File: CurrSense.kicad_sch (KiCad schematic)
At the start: 13 parts

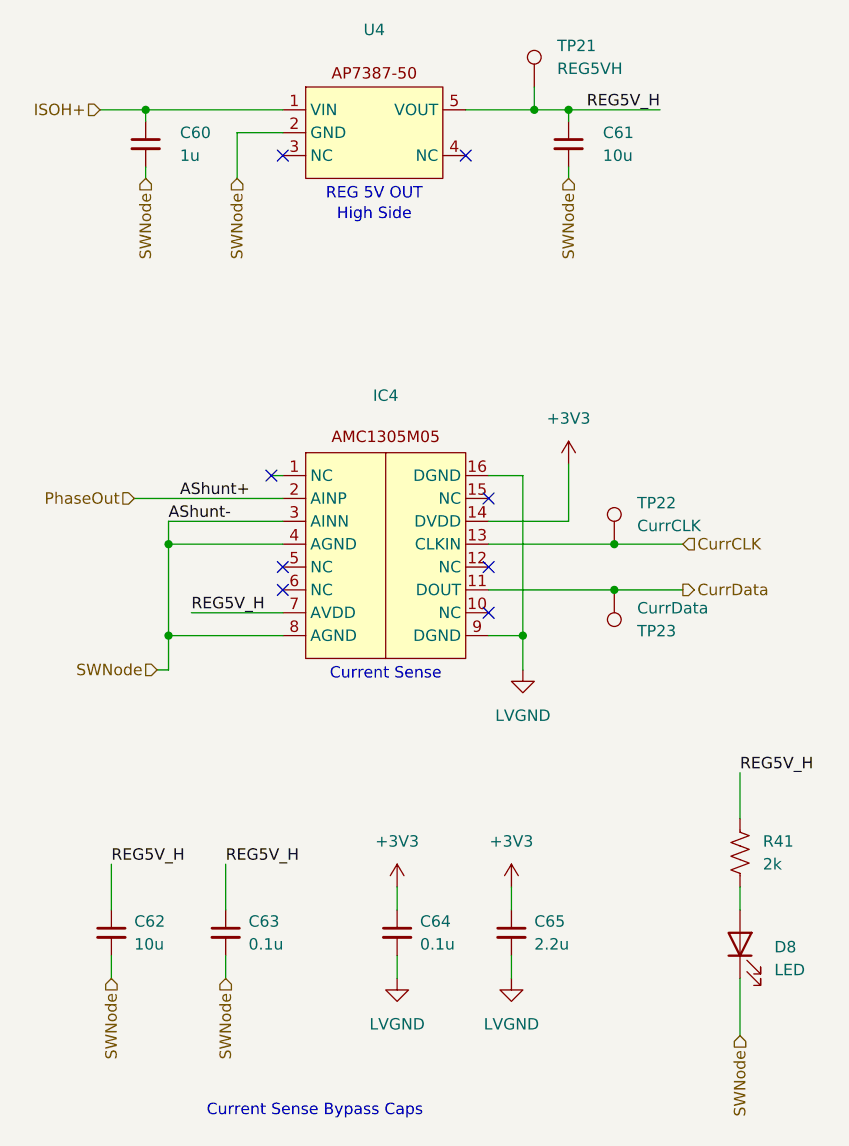
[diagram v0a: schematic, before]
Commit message: new bulk caps, new HV+,- connector placement
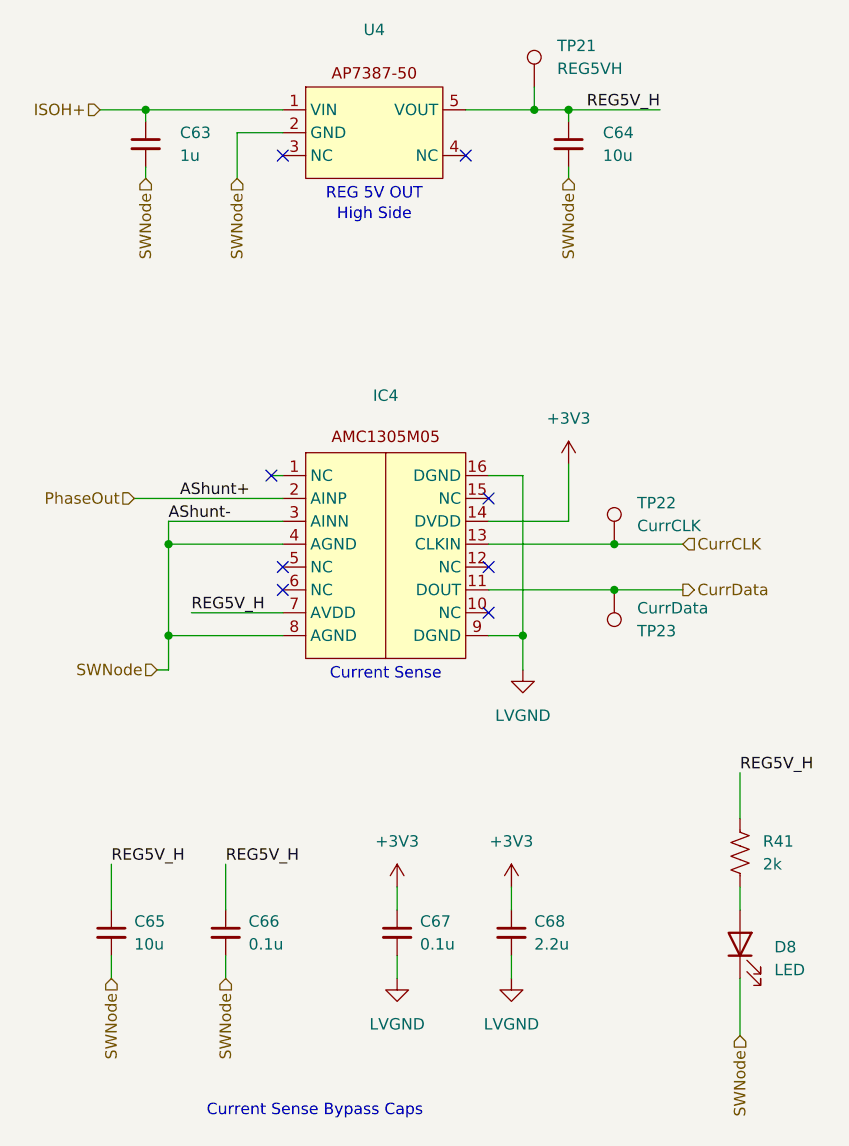
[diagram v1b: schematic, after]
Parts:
- renumbered C60 to C63, C61 to C64, C62 to C65, C63 to C66, C64 to C67, C65 to C68

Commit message: killed testpoints
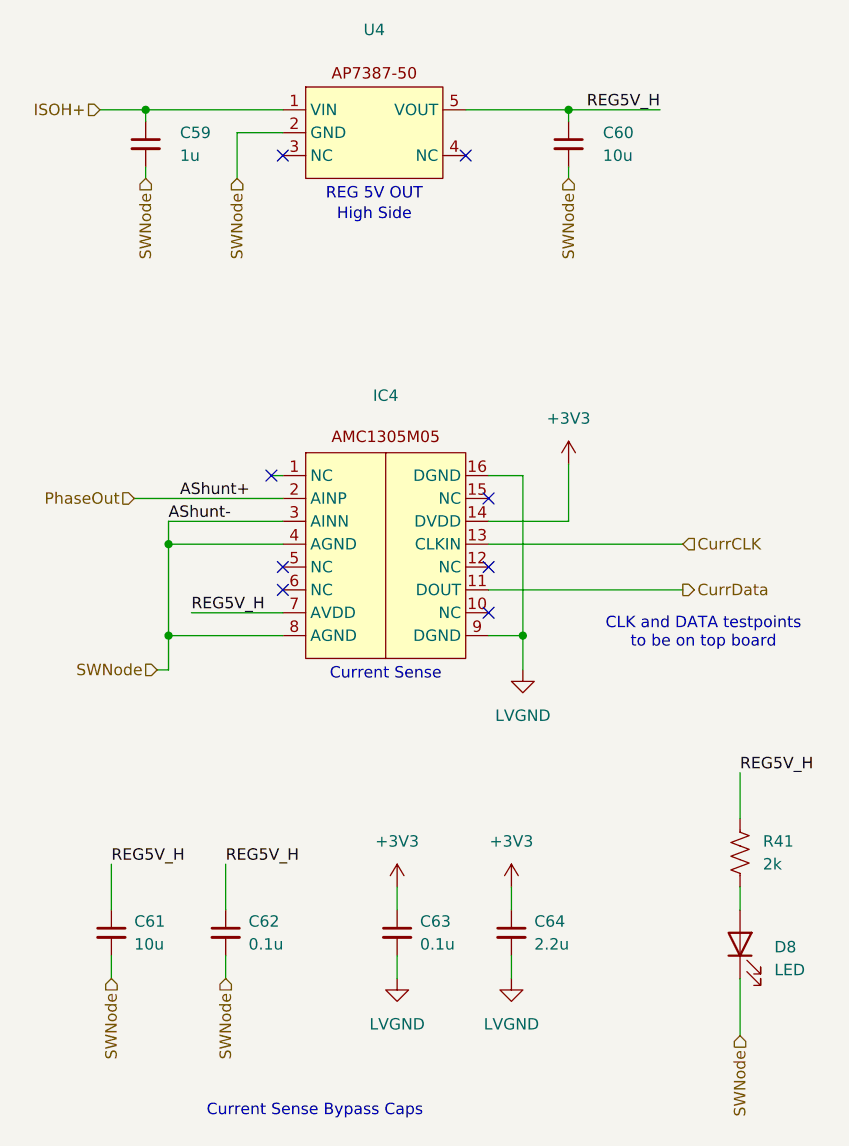
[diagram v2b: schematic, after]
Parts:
- removed TP21: REG5VH, TractionInverter:KEYSTONE_5281, symbol Connector:TestPoint
- removed TP22: CurrCLK, TractionInverter:KEYSTONE_5281, symbol Connector:TestPoint
- removed TP23: CurrData, TractionInverter:KEYSTONE_5281, symbol Connector:TestPoint
- renumbered C63 to C59, C64 to C60, C65 to C61, C66 to C62, C67 to C63, C68 to C64
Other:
- note added: "CLK and DATA testpoints to be on top board"
